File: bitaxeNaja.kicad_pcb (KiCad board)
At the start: 6 copper layers, 65 x 112 mm, 197 parts, among them J1 XT30, J2 Conn_01x08, J3 Conn_01x04, J4 USB_C_Receptacle_USB2.0, J7 Conn_01x04, J8 TC2030-IDC, SW1 SWITCH-SPST, SW2 SWITCH-SPST, U1 TPS546D24ARVFR, U11 MCP1824, U12 MCP1824, U13 EMC2103-2, U2 SN74AVC4T774, U3 TPSM861253RDXR, U4 TPS546D24ARVFR, U5 L78L05_SOT89, U6 ESP32-S3-WROOM-1, U8 25MHz

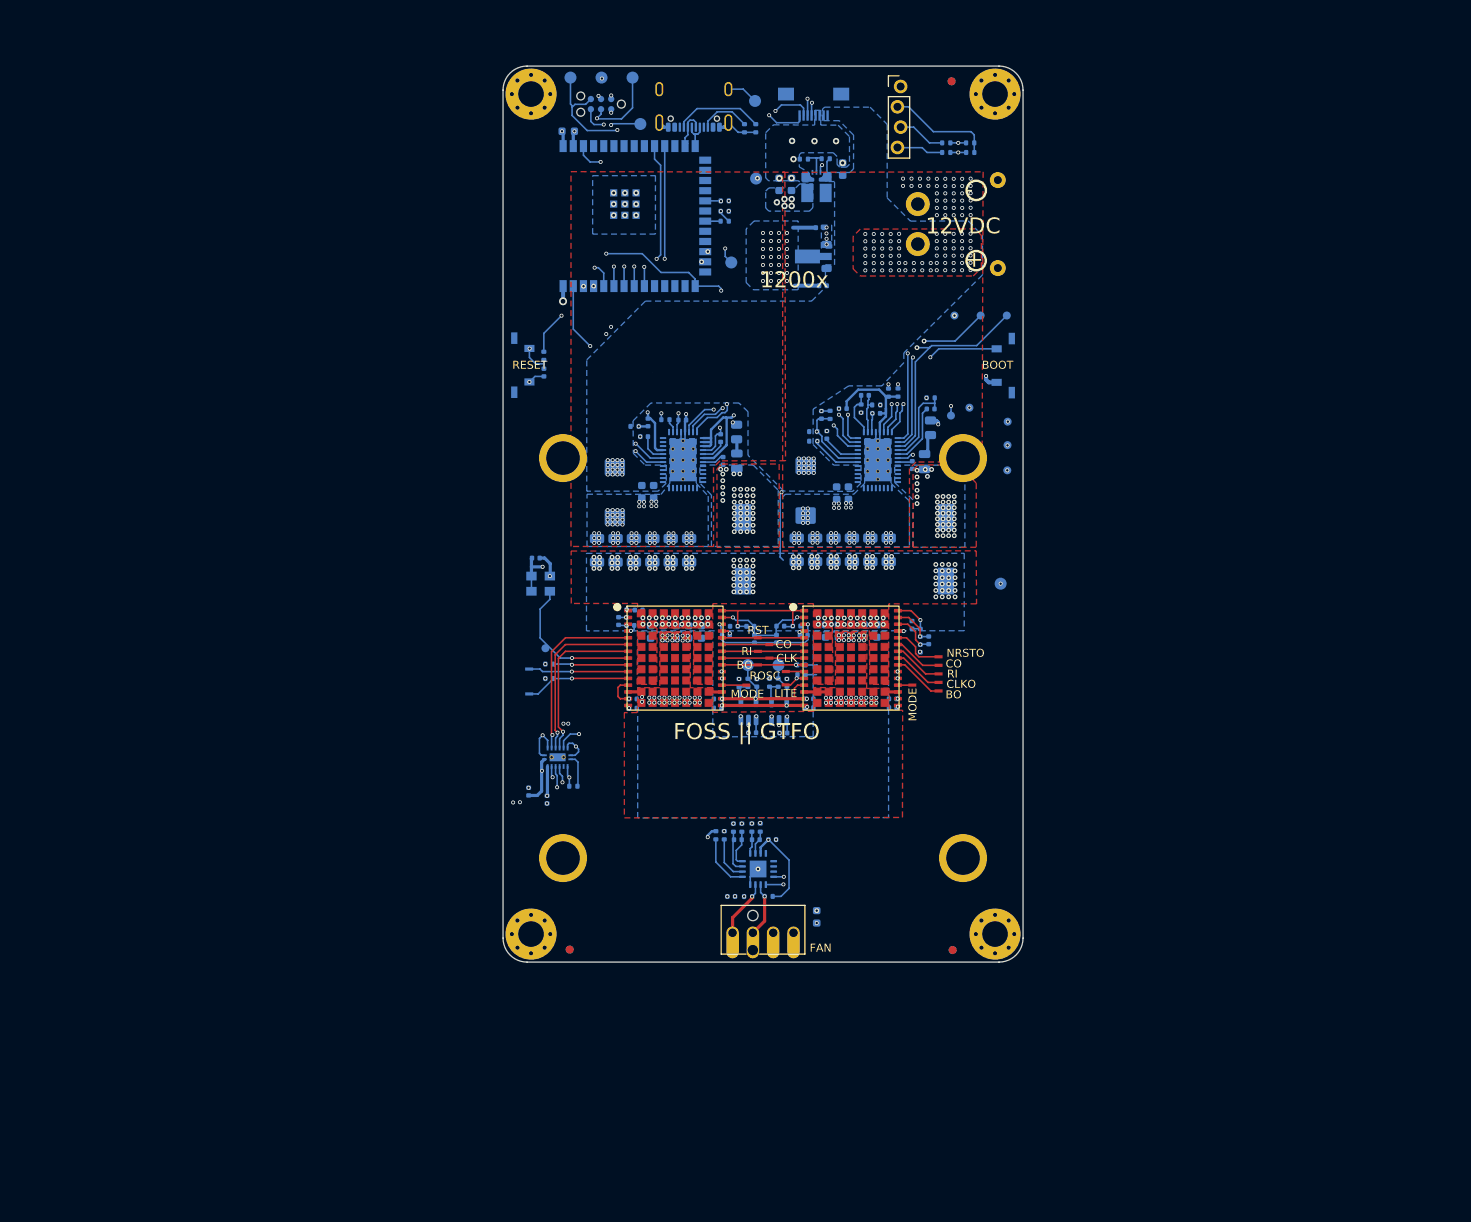
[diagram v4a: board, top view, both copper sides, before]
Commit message: switched to single phase TPS546D24 and put the ASICs in series.
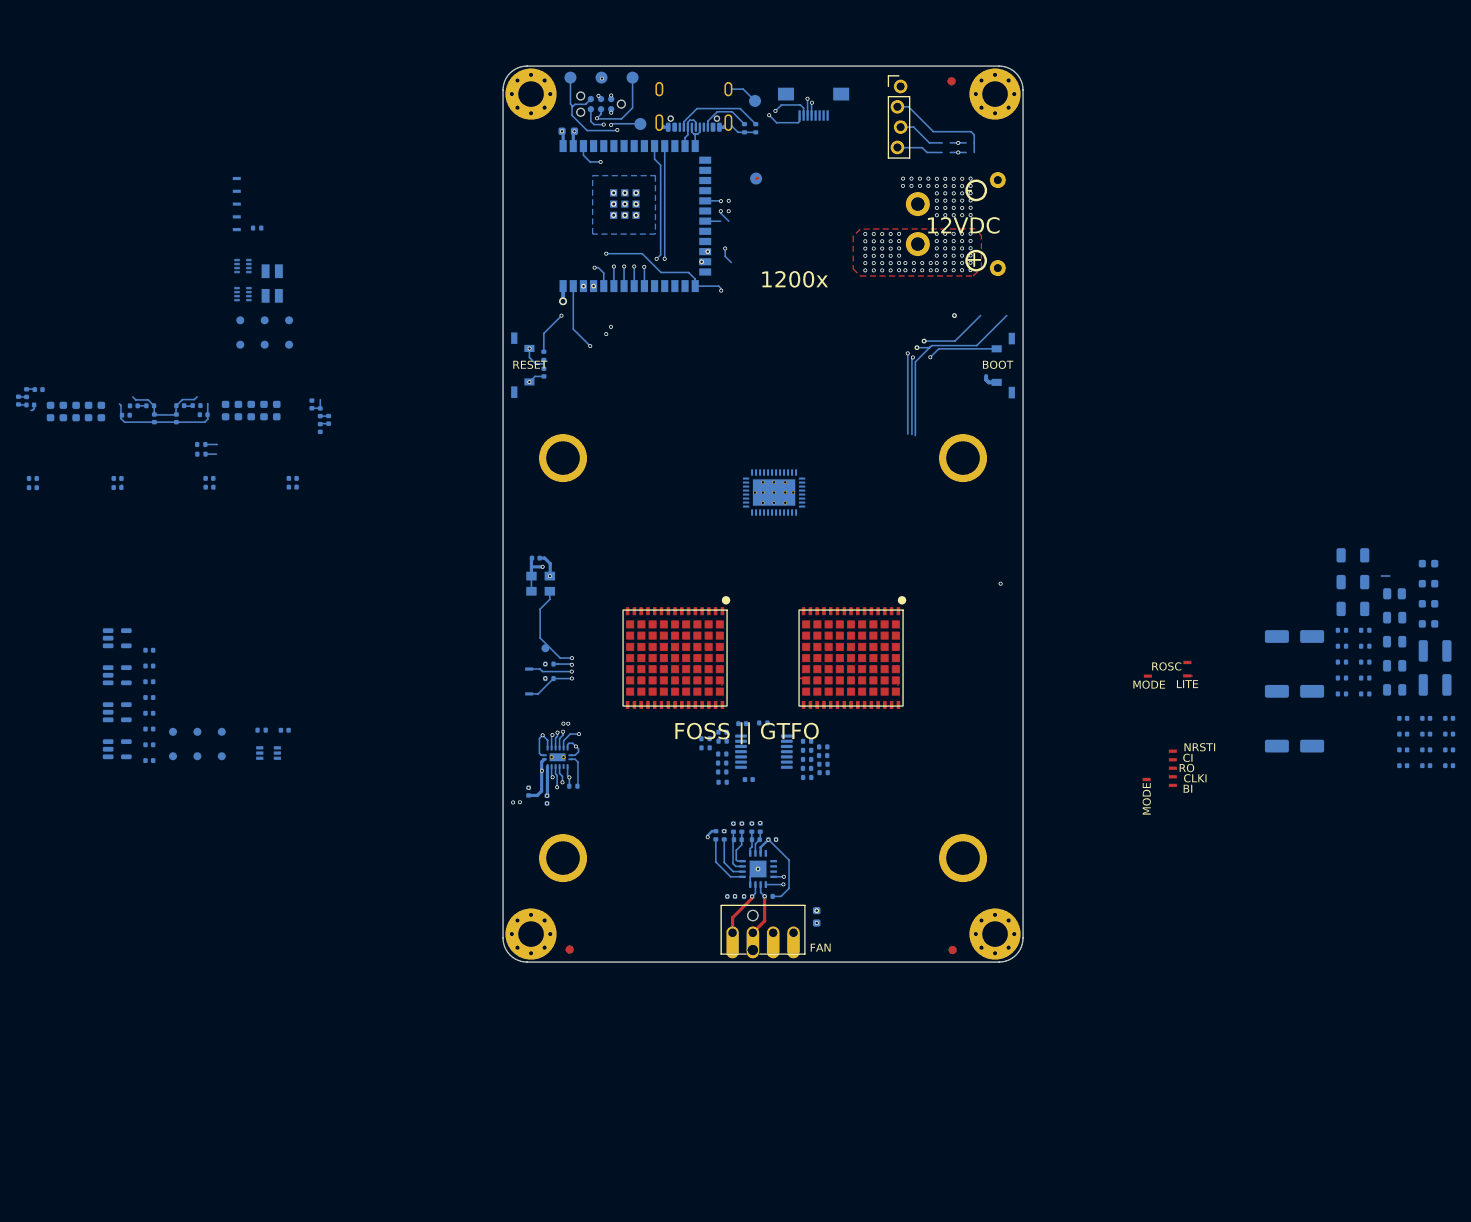
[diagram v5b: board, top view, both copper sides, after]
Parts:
- removed C20, C45: 33pF, Capacitor_SMD:C_0402_1005Metric
- removed C28: 0.1uF, Capacitor_SMD:C_0402_1005Metric
- removed C31, C32, C33: 100uF, Capacitor_SMD:C_1206_3216Metric
- removed C44: 10uF, Capacitor_SMD:C_0603_1608Metric
- removed C46, C47: 1uF, Capacitor_SMD:C_0402_1005Metric
- removed L1: 230nH, bitaxe:FP1107R1
- removed NT2: NetTie_2, bitaxe:NetTie-2_SMD_Pad0.2mmx1mm
- removed R1: 49.9, Resistor_SMD:R_0402_1005Metric
- removed R11: 46.4k, Resistor_SMD:R_0402_1005Metric
- removed R19: 10k, Resistor_SMD:R_0402_1005Metric
- removed R2: 1, Resistor_SMD:R_0805_2012Metric
- removed R21, R22, R40: 4.7k, Resistor_SMD:R_0402_1005Metric
- removed R39: 0, Resistor_SMD:R_0402_1005Metric
- removed R4: 6.04k, Resistor_SMD:R_0402_1005Metric
- removed R41: 38.3k, Resistor_SMD:R_0402_1005Metric
- removed R42, R44: 20k, Resistor_SMD:R_0402_1005Metric
- removed R43: 19.1k, Resistor_SMD:R_0402_1005Metric
- removed TP3: BCX_CLK, TestPoint:TestPoint_Pad_D1.0mm
- removed TP31: BCX_DAT, TestPoint:TestPoint_Pad_D1.0mm
- removed TP37: CO, bitaxe:TestPoint_Pad_1.0x0.4mm
- removed TP38: RI, bitaxe:TestPoint_Pad_1.0x0.4mm
- removed TP39: CLK, bitaxe:TestPoint_Pad_1.0x0.4mm
- removed TP40: BO, bitaxe:TestPoint_Pad_1.0x0.4mm
- removed U1: TPS546D24ARVFR, bitaxe:LQFN40-CLIP
- added C206: 0.1uF, Capacitor_SMD:C_0402_1005Metric, B.Cu at (128.4, 120.2)
- added C207: 1uF, Capacitor_SMD:C_0402_1005Metric, B.Cu at (129.2, 127.2)
- added C6: 4.7uF, Capacitor_SMD:C_1206_3216Metric, B.Cu at (204.7, 105.9)
- added C63: 1uF, Capacitor_SMD:C_0402_1005Metric, B.Cu at (54.3, 124.8)
- added C96: 1uF, Capacitor_SMD:C_0402_1005Metric, B.Cu at (54.3, 115.0)
- added C97: 1uF, Capacitor_SMD:C_0402_1005Metric, B.Cu at (54.3, 113.0)
- added C98: 1uF, Capacitor_SMD:C_0402_1005Metric, B.Cu at (54.3, 111.0)
- added L3: 1.5uH, bitaxe:IND-SMD_L2.0-W1.6, B.Cu at (69.6, 63.6)
- added R12: 30.9k, Resistor_SMD:R_0402_1005Metric, B.Cu at (203.4, 108.5)
- added R55: 1k, Resistor_SMD:R_0402_1005Metric, B.Cu at (126.0, 127.5)
- added R56: 10k, Resistor_SMD:R_0402_1005Metric, B.Cu at (125.9, 125.1)
- added R57: 10k, Resistor_SMD:R_0402_1005Metric, B.Cu at (125.9, 124.0)
- added R58: 1k, Resistor_SMD:R_0402_1005Metric, B.Cu at (125.9, 121.3)
- added R59: 10k, Resistor_SMD:R_0402_1005Metric, B.Cu at (123.8, 123.2)
- added R60: 10k, Resistor_SMD:R_0402_1005Metric, B.Cu at (123.8, 122.1)
- added R61: 1k, Resistor_SMD:R_0402_1005Metric, B.Cu at (138.5, 123.1)
- added R62: 10k, Resistor_SMD:R_0402_1005Metric, B.Cu at (136.5, 123.5)
- added R63: 10k, Resistor_SMD:R_0402_1005Metric, B.Cu at (138.5, 124.2)
- added R64: 1k, Resistor_SMD:R_0402_1005Metric, B.Cu at (136.5, 125.8)
- added R65: 10k, Resistor_SMD:R_0402_1005Metric, B.Cu at (136.5, 126.9)
- added R66: 10k, Resistor_SMD:R_0402_1005Metric, B.Cu at (138.6, 126.3)
- added R67: 0, Resistor_SMD:R_0402_1005Metric, B.Cu at (131.0, 120.1)
- added R68: 1k, Resistor_SMD:R_0402_1005Metric, B.Cu at (125.9, 126.2)
- added R69: 1k, Resistor_SMD:R_0402_1005Metric, B.Cu at (126.0, 122.4)
- added R70: 1k, Resistor_SMD:R_0402_1005Metric, B.Cu at (136.5, 122.4)
- added R71: 1k, Resistor_SMD:R_0402_1005Metric, B.Cu at (136.5, 124.7)
- added R72: 1k, Resistor_SMD:R_0402_1005Metric, B.Cu at (138.6, 125.3)
- added TP14: 3V3, bitaxe:TestPoint_Pad_D1.0mm, B.Cu at (65.7, 69.8)
- added TP16: VDD, bitaxe:TestPoint_Pad_D1.0mm, B.Cu at (68.7, 69.8)
- added TP17: BO, bitaxe:TestPoint_Pad_1.0x0.4mm, B.Cu at (65.2, 58.4)
- added TP20: GND, bitaxe:TestPoint_Pad_D1.0mm, B.Cu at (71.8, 72.8)
- added TP21: GND, bitaxe:TestPoint_Pad_D1.0mm, B.Cu at (71.8, 69.8)
- added TP28: 0V8, bitaxe:TestPoint_Pad_D1.0mm, B.Cu at (63.3, 124.3)
- added U10: TLV77308PDBVR, Package_TO_SOT_SMD:SOT-23-5, B.Cu at (50.3, 123.4)
- added U14: TLV77312PDBVR, Package_TO_SOT_SMD:SOT-23-5, B.Cu at (50.3, 109.5)
- added U17: TLV3544, Package_SO:TSSOP-14_4.4x5mm_P0.65mm, B.Cu at (131.1, 123.7)
- added U9: TPS22919DCKR, bitaxe:DCK0006A_N, B.Cu at (69.2, 123.9)
- C1: value 33uF -> 68uF; footprint Capacitor_Tantalum_SMD:CP_EIA-7343-31_Kemet-D -> Capacitor_SMD:CP_Elec_5x5.8
- C10, C9: value 100uF -> 1uF; footprint Capacitor_SMD:C_1206_3216Metric -> Capacitor_SMD:C_0603_1608Metric
- C11: value 100uF -> 4.7uF; footprint Capacitor_SMD:C_1206_3216Metric -> Capacitor_SMD:C_0402_1005Metric
- C12: value 100uF -> 10uF; footprint Capacitor_SMD:C_1206_3216Metric -> Capacitor_SMD:C_0603_1608Metric
- C13: value 100uF -> 4.7nF; footprint Capacitor_SMD:C_1206_3216Metric -> Capacitor_SMD:C_0402_1005Metric
- C14: value 100uF -> 2.2nF; footprint Capacitor_SMD:C_1206_3216Metric -> Capacitor_SMD:C_0402_1005Metric
- C16, C37: value 4.7uF -> 0.1uF
- C17: value 0.1uF -> 1000pF; footprint Capacitor_SMD:C_0402_1005Metric -> Capacitor_SMD:C_0805_2012Metric
- C19: value 1uF -> 4.7uF; footprint Capacitor_SMD:C_0402_1005Metric -> Capacitor_SMD:C_1206_3216Metric
- C2, C3: value 10uF -> 68uF; footprint Capacitor_SMD:C_0603_1608Metric -> Capacitor_SMD:CP_Elec_5x5.8
- C22: value 33uF -> 47uF; footprint Capacitor_Tantalum_SMD:CP_EIA-7343-31_Kemet-D -> Capacitor_SMD:C_0805_2012Metric
- C23, C24: value 10uF -> 100uF; footprint Capacitor_SMD:C_0603_1608Metric -> Capacitor_SMD:C_1210_3225Metric
- C29: value 1000pF -> 33nF; footprint Capacitor_SMD:C_0805_2012Metric -> Capacitor_SMD:C_0402_1005Metric
- C30: value 100uF -> 33nF; footprint Capacitor_SMD:C_1206_3216Metric -> Capacitor_SMD:C_0402_1005Metric
- C34: value 100uF -> 1uF; footprint Capacitor_SMD:C_1206_3216Metric -> Capacitor_SMD:C_0402_1005Metric
- C35: value 100uF -> 22uF; footprint Capacitor_SMD:C_1206_3216Metric -> Capacitor_SMD:C_0805_2012Metric
- C36: value 1uF -> 22uF; footprint Capacitor_SMD:C_0402_1005Metric -> Capacitor_SMD:C_0805_2012Metric
- C39, C43: value 10uF -> 0.1uF; footprint Capacitor_SMD:C_0603_1608Metric -> Capacitor_SMD:C_0402_1005Metric
- C42: value 1uF -> 0.1uF
- C7: value 0.1uF -> 4.7uF; footprint Capacitor_SMD:C_0402_1005Metric -> Capacitor_SMD:C_1206_3216Metric
- C8: value 1000pF -> 10uF; footprint Capacitor_SMD:C_0805_2012Metric -> Capacitor_SMD:C_0603_1608Metric
- L2: value 230nH -> 1.5uH; footprint bitaxe:FP1107R1 -> bitaxe:IND-SMD_L2.0-W1.6
- R13: value 31.6k -> 10k
- R15: value 1 -> 13.7k; footprint Resistor_SMD:R_0805_2012Metric -> Resistor_SMD:R_0402_1005Metric
- R16, R3: value 10 -> 10k
- R17: value 20k -> 52.3k
- R18: value 10k -> 1k
- R37: value 0 -> 10k
- R38: value 0 -> 1k
- R5: value 649 -> 10
- R6: value 10k -> 1; footprint Resistor_SMD:R_0402_1005Metric -> Resistor_SMD:R_0805_2012Metric
- R7: value 31.6k -> 49.9
- TP1: value TestPoint -> PWR EN; footprint TestPoint:TestPoint_Pad_D1.0mm -> bitaxe:TestPoint_Pad_D1.0mm
- TP15: value Vcore -> 5V; footprint TestPoint:TestPoint_Pad_D1.5mm -> bitaxe:TestPoint_Pad_D1.0mm
- TP18: value 1V2 -> CLKO; footprint TestPoint:TestPoint_Pad_D1.5mm -> bitaxe:TestPoint_Pad_1.0x0.4mm
- TP19: value 0V8 -> RI; footprint TestPoint:TestPoint_Pad_D1.5mm -> bitaxe:TestPoint_Pad_1.0x0.4mm
- TP22: value ALRT_VR -> CO; footprint TestPoint:TestPoint_Pad_D1.0mm -> bitaxe:TestPoint_Pad_1.0x0.4mm
- TP23: value SDA_VR -> NRSTO; footprint TestPoint:TestPoint_Pad_D1.0mm -> bitaxe:TestPoint_Pad_1.0x0.4mm
- TP24: value SCL_VR -> GND; footprint TestPoint:TestPoint_Pad_D1.0mm -> bitaxe:TestPoint_Pad_D1.0mm
- TP25: value GND -> 0V8; footprint TestPoint:TestPoint_Pad_D1.0mm -> bitaxe:TestPoint_Pad_D1.0mm
- TP26: value RST -> 1V2; footprint bitaxe:TestPoint_Pad_1.0x0.4mm -> bitaxe:TestPoint_Pad_D1.0mm; moved to B.Cu
- TP27: value 5V -> GND; footprint TestPoint:TestPoint_Pad_D1.5mm -> bitaxe:TestPoint_Pad_D1.0mm
- TP30: value BCX_CLK -> 1V2; footprint TestPoint:TestPoint_Pad_D1.0mm -> bitaxe:TestPoint_Pad_D1.0mm
- TP5: value BO -> BI
- TP6: value CLKO -> CLKI
- TP7: value RI -> RO
- TP8: value CO -> CI
- TP9: value NRSTO -> NRSTI
- U11: value MCP1824 -> TLV77312PDBVR
- U12: value MCP1824 -> TLV77308PDBVR
- U3: value TPSM861253RDXR -> TPS546D24SRVFR; footprint bitaxe:TPSM863257RDX -> bitaxe:LQFN40-CLIP
- U4: value TPS546D24ARVFR -> TPS62933DRLR; footprint bitaxe:LQFN40-CLIP -> bitaxe:SOT-583-8_L2.1-W1.2-P0.50-LS1.6-BR
- U5: value L78L05_SOT89 -> TPS62933DRLR; footprint Package_TO_SOT_SMD:SOT-89-3 -> bitaxe:SOT-583-8_L2.1-W1.2-P0.50-LS1.6-BR
- moved TP24 117.9 mm to (57.2, 124.3), turned to 0 degrees
- moved TP25 109.3 mm to (57.2, 121.2), turned to 0 degrees
- moved C37 108.7 mm to (216.8, 125.4)
- moved C43 105.9 mm to (216.8, 119.5), turned to 0 degrees
- moved C39 105.0 mm to (216.8, 123.5), turned to 0 degrees
- moved TP30 101.9 mm to (63.3, 121.2), turned to 0 degrees
- moved C24 101.1 mm to (215.0, 111.1), turned to 0 degrees
- moved C23 100.6 mm to (215.0, 115.4), turned to 0 degrees
- moved C35 100.4 mm to (210.0, 110.0), turned to 0 degrees
- moved C22 99.9 mm to (210.0, 113.0), turned to 0 degrees
- moved R18 98.4 mm to (68.3, 121.0)
- moved C42 98.3 mm to (216.8, 121.5), turned to 0 degrees
- moved R6 97.1 mm to (209.9, 104.0)
- moved TP15 96.7 mm to (68.7, 72.8)
- moved C36 96.5 mm to (210.0, 106.9), turned to 0 degrees
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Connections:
- A1 pad 12: /ASIC/0V8_1 -> /ASIC/0V8_0
- A1 pad 14: /ASIC/0V8_1 -> /ASIC/0V8_0
- A1 pad 15: /ASIC/1V2_1 -> /ASIC/1V2_0
- A1 pad 16: /ASIC/1V2 -> /ASIC/1V2_0
- A1 pad 17: /ASIC/0V8 -> /ASIC/0V8_0
- A1 pad 22: Net-(A1-BO) -> /ASIC/Level Shifter/BI
- A1 pad 23: Net-(A1-CLKO) -> /ASIC/Level Shifter/CLKI
- A1 pad 24: Net-(A1-RI) -> /ASIC/Level Shifter/RO
- A1 pad 25: Net-(A1-CO) -> /ASIC/Level Shifter/CI
- A1 pad 26: Net-(A1-NRSTO) -> /ASIC/Level Shifter/NRSTI
- A1 pad 27: GND -> Net-(A1-VSS-Pad27)
- A1 pad 31: /Vcore -> /ASIC/GND_1
- A2 pad 1: Net-(A1-VDD3_1) -> Net-(A2-VDD3_0)
- A2 pad 12: /ASIC/0V8 -> Net-(A2-INV_CLKO)
- A2 pad 13: GND -> /ASIC/GND_1
- A2 pad 14: /ASIC/0V8 -> Net-(A2-INV_CLKO)
- A2 pad 15: /ASIC/1V2 -> Net-(A2-VDDIO_12_0)
- A2 pad 16: /ASIC/1V2_2 -> /ASIC/1V2_1
- A2 pad 17: /ASIC/0V8_2 -> /ASIC/0V8_1
- A2 pad 18: GND -> /ASIC/GND_1
- A2 pad 19: Net-(A2-PIN_MODE) -> /ASIC/GND_1
- A2 pad 2: Net-(A1-VDD2_1) -> Net-(A2-VDD2_0)
- A2 pad 22: Net-(A2-BO) -> /ASIC/Level Shifter/NRSTI2
- A2 pad 23: Net-(A2-CLKO) -> /ASIC/Level Shifter/CI2
- A2 pad 24: Net-(A2-RI) -> /ASIC/Level Shifter/RO2
- A2 pad 25: Net-(A2-CO) -> /ASIC/Level Shifter/CLKO
- A2 pad 26: Net-(A2-NRSTO) -> /ASIC/Level Shifter/BI2
- A2 pad 27: GND -> /ASIC/GND_1
- A2 pad 3: Net-(A1-VDD1_1) -> Net-(A2-VDD1_0)
- A2 pad 31: /Vcore -> /VDD
- A2 pad 32: GND -> /ASIC/GND_1
- A2 pad 4: GND -> /ASIC/GND_1
- A2 pad 5: Net-(A1-NRSTO) -> unconnected-(A2-BO-Pad5)
- A2 pad 6: Net-(A1-CO) -> unconnected-(A2-CLKO-Pad6)
- A2 pad 7: Net-(A1-RI) -> Net-(A2-RI)
- A2 pad 8: Net-(A1-CLKO) -> unconnected-(A2-CO-Pad8)
- A2 pad 9: Net-(A1-BO) -> unconnected-(A2-NRSTO-Pad9)
- C10 pad 1: GND -> /Power/AGND
- C10 pad 2: /Vcore -> Net-(U3-AVIN)
- C11 pad 2: /Vcore -> /Power/V5reg_1
- C12 pad 2: /Vcore -> /12V
- C13 pad 1: GND -> /12V
- C13 pad 2: /Vcore -> GND
- C14 pad 1: GND -> /12V
- C14 pad 2: /Vcore -> GND
- C15 pad 1: /Power/AGND1 -> /Power/BP1v5
- C15 pad 2: Net-(U1-AVIN) -> Net-(U3-DRTN)
- C16 pad 1: GND -> Net-(U3-BOOT)
- C16 pad 2: /Power/V5reg_1 -> /Power/SW1
- C17 pad 1: /Power/EN_UVLO -> /Power/SW1
- C17 pad 2: GND -> Net-(C17-Pad2)
- C18 pad 1: Net-(U1-VOSNS) -> Net-(U3-VOSNS)
- C18 pad 2: Net-(U1-GOSNS) -> Net-(U3-GOSNS)
- C19 pad 1: /Power/BP1v5_1 -> /12V
- C19 pad 2: Net-(U1-DRTN) -> GND
- C22 pad 1: /12V -> GND
- C22 pad 2: GND -> /VDD
- C23 pad 1: /12V -> GND
- C23 pad 2: GND -> /VDD
- C24 pad 1: /12V -> GND
- C24 pad 2: GND -> /VDD
- C29 pad 1: /Power/SW2 -> GND
- C29 pad 2: Net-(C29-Pad2) -> Net-(U4-SS)
- C30 pad 2: /Vcore -> Net-(U5-SS)
- C34 pad 1: GND -> /5V
- C34 pad 2: /Vcore -> GND
- C35 pad 2: /Vcore -> /3V3
- C36 pad 1: /Power/AGND2 -> GND
- C36 pad 2: Net-(U4-AVIN) -> /5V
- C37 pad 1: GND -> /12V
- C37 pad 2: /Power/V5reg_2 -> GND
- C38 pad 1: /Vcore -> /ASIC/GND_1
- C42 pad 1: /Power/BP1v5_2 -> Net-(U4-BST)
- C42 pad 2: Net-(U4-DRTN) -> Net-(U4-SW)
- C43 pad 1: /3V3 -> Net-(U5-BST)
- C43 pad 2: GND -> Net-(U5-SW)
- C51 pad 1: /ASIC/1V2 -> /ASIC/1V2_0
- C53 pad 1: /ASIC/1V2 -> /ASIC/1V2_0
- C54 pad 1: /Vcore -> /ASIC/GND_1
- C55 pad 1: /Vcore -> /ASIC/GND_1
- C56 pad 1: /Vcore -> /ASIC/GND_1
- C57 pad 1: /Vcore -> /ASIC/GND_1
- C58 pad 1: /Vcore -> /VDD
- C58 pad 2: GND -> /ASIC/GND_1
- C59 pad 1: /Vcore -> /VDD
- C59 pad 2: GND -> /ASIC/GND_1
- C60 pad 1: /Vcore -> /VDD
- C60 pad 2: GND -> /ASIC/GND_1
- C61 pad 1: /Vcore -> /VDD
- C61 pad 2: GND -> /ASIC/GND_1
- C62 pad 1: /Vcore -> /VDD
- C62 pad 2: GND -> /ASIC/GND_1
- C67 pad 2: /Vcore -> /ASIC/GND_1
- C68 pad 1: /Vcore -> /ASIC/GND_1
- C7 pad 1: Net-(U1-BOOT) -> /12V
- C7 pad 2: /Power/SW1 -> GND
- C71 pad 2: GND -> Net-(A1-VSS-Pad27)
- C72 pad 1: GND -> /ASIC/GND_1
- C72 pad 2: Net-(A1-VDD1_1) -> Net-(A2-VDD1_0)
- C73 pad 1: Net-(A1-VDD1_1) -> Net-(A2-VDD1_0)
- C73 pad 2: Net-(A1-VDD2_1) -> Net-(A2-VDD2_0)
- C74 pad 1: Net-(A1-VDD2_1) -> Net-(A2-VDD2_0)
- C74 pad 2: Net-(A1-VDD3_1) -> Net-(A2-VDD3_0)
- C75 pad 1: Net-(A1-VDD3_1) -> Net-(A2-VDD3_0)
- C75 pad 2: /Vcore -> /VDD
- C76 pad 1: /Vcore -> /VDD
- C79 pad 2: GND -> /ASIC/GND_1
- C8 pad 1: /Power/SW1 -> GND
- C8 pad 2: Net-(C8-Pad2) -> /12V
- C80 pad 2: /ASIC/0V8_1 -> /ASIC/0V8_0
- C81 pad 2: /ASIC/1V2_1 -> /ASIC/1V2_0
- C82 pad 2: /ASIC/0V8 -> /ASIC/0V8_0
- C83 pad 2: /ASIC/1V2 -> /ASIC/1V2_0
- C84 pad 1: GND -> /ASIC/GND_1
- C84 pad 2: /ASIC/1V2 -> Net-(A2-VDDIO_12_0)
- C85 pad 1: GND -> /ASIC/GND_1
- C85 pad 2: /ASIC/0V8 -> Net-(A2-INV_CLKO)
- C86 pad 1: GND -> /ASIC/GND_1
- C86 pad 2: /ASIC/1V2_2 -> /ASIC/1V2_1
- C87 pad 1: GND -> /ASIC/GND_1
- C87 pad 2: /ASIC/0V8_2 -> /ASIC/0V8_1
- C88 pad 2: /5V -> /ASIC/5V_SWITCH
- C89 pad 2: /ASIC/1V2 -> /ASIC/0V8_0
- C9 pad 1: GND -> /12V
- C9 pad 2: /Vcore -> GND
- C90 pad 2: /5V -> /ASIC/1V2_0
- C91 pad 1: GND -> /ASIC/GND_1
- C91 pad 2: /ASIC/0V8 -> /ASIC/5V_SWITCH
- L2 pad 1: /Power/SW2 -> Net-(U4-SW)
- L2 pad 2: /Vcore -> /3V3
- NT1 pad 2: /Power/AGND1 -> /Power/AGND
- R13 pad 1: /Power/AGND1 -> GND
- R13 pad 2: Net-(U1-VSEL) -> Net-(U4-FB)
- R15 pad 1: Net-(C29-Pad2) -> GND
- R15 pad 2: GND -> Net-(U4-RT)
- R16 pad 1: /12V -> GND
- R16 pad 2: Net-(U4-AVIN) -> Net-(U5-RT)
- R17 pad 1: Net-(U3-EN) -> Net-(U5-FB)
- R17 pad 2: /12V -> /5V
- R18 pad 1: GND -> /ESP32/5V_SWITCH
- R18 pad 2: Net-(U3-EN) -> Net-(U9-QOD)
- R27 pad 2: Net-(A1-BO) -> /ASIC/Level Shifter/BI
- R28 pad 1: GND -> /ASIC/GND_1
- R3 pad 1: /12V -> GND
- R3 pad 2: Net-(U1-AVIN) -> /ESP32/PWR_EN
- R37 pad 1: /ESP32/SMB_ALRT -> GND
- R37 pad 2: /Power/ALRT_VR -> Net-(U5-FB)
- R38 pad 1: /ESP32/SDA -> Net-(A2-RI)
- R38 pad 2: /Power/SDA_VR -> /ASIC/1V2_1
- R5 pad 1: GND -> /12V
- R5 pad 2: /Power/EN_UVLO -> Net-(U3-AVIN)
- R6 pad 1: /Power/PGOOD -> Net-(C17-Pad2)
- R6 pad 2: /3V3 -> GND
- R7 pad 1: Net-(U1-MSEL1) -> /VDD
- R7 pad 2: /Power/BP1v5_1 -> Net-(U3-VOSNS)
- R8 pad 1: Net-(U1-GOSNS) -> Net-(U3-GOSNS)
- TP1 pad 1: Net-(U1-ADRSEL) -> /ESP32/PWR_EN
- TP15 pad 1: /Vcore -> /5V
- TP18 pad 1: /ASIC/1V2 -> /ASIC/Level Shifter/CLKI
- TP19 pad 1: /ASIC/0V8 -> /ASIC/Level Shifter/RO
- TP22 pad 1: /Power/ALRT_VR -> /ASIC/Level Shifter/CI
- TP23 pad 1: /Power/SDA_VR -> /ASIC/Level Shifter/NRSTI
- TP24 pad 1: /Power/SCL_VR -> GND
- TP25 pad 1: GND -> /ASIC/0V8_0
- TP26 pad 1: Net-(A1-NRSTO) -> /ASIC/1V2_0
- TP27 pad 1: /5V -> /ASIC/GND_1
- TP30 pad 1: /Power/BCX_CLK -> /ASIC/1V2_1
- TP42 pad 1: Net-(A2-PIN_MODE) -> /ASIC/GND_1
- TP5 pad 1: Net-(A2-BO) -> /ASIC/Level Shifter/BI2
- TP6 pad 1: Net-(A2-CLKO) -> /ASIC/Level Shifter/CLKO
- TP7 pad 1: Net-(A2-RI) -> /ASIC/Level Shifter/RO2
- TP8 pad 1: Net-(A2-CO) -> /ASIC/Level Shifter/CI2
- TP9 pad 1: Net-(A2-NRSTO) -> /ASIC/Level Shifter/NRSTI2
- U11 pad 1: /5V -> /ASIC/5V_SWITCH
- U11 pad 3: /5V -> /ASIC/5V_SWITCH
- U11 pad 4: Net-(U11-ADJ) -> unconnected-(U11-NC-Pad4)
- U11 pad 5: /ASIC/1V2 -> /ASIC/1V2_0
- U12 pad 1: /5V -> /ASIC/5V_SWITCH
- U12 pad 2: GND -> /ASIC/GND_1
- U12 pad 3: /5V -> /ASIC/5V_SWITCH
- U12 pad 4: Net-(U12-ADJ) -> unconnected-(U12-NC-Pad4)
- U12 pad 5: /ASIC/0V8 -> /ASIC/0V8_1
- U2 pad 16: /ASIC/1V2 -> /ASIC/1V2_0
- U3 pad 1: /12V -> /Power/PGOOD
- U3 pad 2: unconnected-(U3-SW-Pad2) -> /ESP32/SDA
- U3 pad 3: /3V3 -> /ESP32/SCL
- U3 pad 4: GND -> /Power/BP1v5
- U3 pad 5: unconnected-(U3-PG-Pad5) -> Net-(U3-DRTN)
- U3 pad 6: Net-(U3-EN) -> /ESP32/SMB_ALRT
- U3 pad 7: /3V3 -> Net-(U3-BOOT)
- U4 pad 1: /Power/AGND2 -> Net-(U4-RT)
- U4 pad 2: /Power/AGND2 -> unconnected-(U4-EN-Pad2)
- U4 pad 3: /Power/AGND2 -> /12V
- U4 pad 4: /Power/BP1v5_2 -> GND
- U4 pad 5: Net-(U4-DRTN) -> Net-(U4-SW)
- U4 pad 6: /Power/AGND2 -> Net-(U4-BST)
- U4 pad 7: Net-(U4-BOOT) -> Net-(U4-SS)
- U4 pad 8: /Power/SW2 -> Net-(U4-FB)
- U5 pad 1: /5V -> Net-(U5-RT)
- U5 pad 2: GND -> unconnected-(U5-EN-Pad2)
- U6 pad 23: unconnected-(U6-GPIO21-Pad23) -> /ESP32/5V_EN
- U6 pad 38: /Vcore -> /VDD
- U8 pad 1: /ASIC/1V2 -> /ASIC/1V2_0
- U8 pad 4: /ASIC/1V2 -> /ASIC/1V2_0
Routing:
- net (no net): track 0.00 -> 178.4 mm, vias 0 -> 8
- net /Vcore: track 73.6 -> 0.00 mm, vias 168 -> 0
- net /Power/SCL_VR: track 72.3 -> 0.00 mm, vias 2 -> 0
- net /Power/ALRT_VR: track 66.9 -> 0.00 mm, vias 3 -> 0
- net /Power/SDA_VR: track 66.6 -> 0.00 mm, vias 3 -> 0
- net /Power/SYNC: track 49.3 -> 0.00 mm, vias 3 -> 0
- net /Power/BCX_DAT: track 49.1 -> 0.00 mm, vias 3 -> 0
- net /ASIC/1V2: track 94.0 -> 46.6 mm, vias 6 -> 3
- net /VDD: track 0.00 -> 42.8 mm, vias 0 -> 1
- net /Power/BCX_CLK: track 42.8 -> 0.00 mm, vias 3 -> 0
- net /Power/AGND2: track 42.3 -> 0.00 mm, vias 3 -> 0
- net /Power/EN_UVLO: track 40.6 -> 0.00 mm, vias 2 -> 0
- net /Power/VSHARE: track 32.9 -> 0.00 mm, vias 2 -> 0
- net /5V: track 162.8 -> 130.9 mm, vias 13 -> 5
- net GND: track 68.2 -> 38.9 mm, vias 302 -> 64
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- removed copper zone on B.Cu, net /12V
- removed copper zone on In2.Cu, net /12V
- removed copper zone on B.Cu, net /3V3
- removed copper zone on B.Cu, net /5V
- removed copper zone on B.Cu, net /Power/SW1
- removed copper zone on F.Cu, net /Power/SW1
- removed copper zone on In2.Cu, net /Power/SW1
- removed copper zone on B.Cu, net /Power/SW2
- removed copper zone on F.Cu, net /Power/SW2
- removed copper zone on In2.Cu, net /Power/SW2
- removed copper zone on B.Cu, net /Vcore
- removed copper zone on F.Cu, net /Vcore
- removed copper zone on In2.Cu, net /Vcore
- removed copper zone on F.Cu, net GND
- removed copper zone on In2.Cu, net GND
- removed copper zone on In3.Cu, net GND

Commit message: rough parts placement.
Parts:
- removed H5, H6, H7, H8: MountingHole_Pad, bitaxe:Sinhoo SMTSO3015CTJ_nopaste
- added C99: 0.1uF, Capacitor_SMD:C_0402_1005Metric, B.Cu at (164.2, 128.8)
- added HS1: Heatsink, bitaxe:Heatsink-5hole-BitaxeGT, F.Cu at (131.0, 112.0)
- added L1: 150nH, bitaxe:GDIM107050-R15S1MTF-0R37, B.Cu at (133.4, 100.5)
- added R73: 0, Resistor_SMD:R_0402_1005Metric, B.Cu at (156.9, 128.5)
- added TP31: CLKI, TestPoint:TestPoint_Pad_D1.0mm, B.Cu at (159.4, 123.5)
- added U1: STHW4-DU-HN050206, bitaxe:PAD-SMD_L5.0-W2.0_STHW4-DU-HN050206, F.Cu at (132.4, 91.3)
- added U15: 25MHz, bitaxe:SMD3225-4P, B.Cu at (160.5, 127.8)
- TP17, TP18, TP19, TP22, TP23: moved to F.Cu
- moved C37 161.8 mm to (75.5, 46.5), turned to 90 degrees
- moved C42 161.2 mm to (76.5, 42.2), turned to 180 degrees
- moved C29 156.9 mm to (78.1, 42.9), turned to -90 degrees
- moved C35 150.9 mm to (73.3, 46.0), turned to 180 degrees
- moved C8 149.2 mm to (77.8, 47.2), turned to 180 degrees
- moved C39 147.4 mm to (82.3, 63.2), turned to 90 degrees
- moved C43 146.6 mm to (83.3, 58.9), turned to 180 degrees
- moved R13 145.4 mm to (79.8, 44.7), turned to 180 degrees
- moved R15 143.9 mm to (79.8, 45.8), turned to 180 degrees
- moved C30 142.2 mm to (84.9, 59.6), turned to -90 degrees
- moved R12 139.6 mm to (79.8, 43.5)
- moved C36 137.3 mm to (80.0, 62.7), turned to 180 degrees
- moved C12 134.4 mm to (84.7, 64.0), turned to 180 degrees
- moved R17 129.9 mm to (86.5, 60.3)
- moved R16 129.9 mm to (86.4, 62.5), turned to 180 degrees
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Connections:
- A1 pad 27: Net-(A1-VSS-Pad27) -> GND
- A2 pad 12: Net-(A2-INV_CLKO) -> /ASIC/0V8_1
- A2 pad 14: Net-(A2-INV_CLKO) -> /ASIC/0V8_1
- A2 pad 15: Net-(A2-VDDIO_12_0) -> /ASIC/1V2_1
- C71 pad 2: Net-(A1-VSS-Pad27) -> GND
- C84 pad 2: Net-(A2-VDDIO_12_0) -> /ASIC/1V2_1
- C85 pad 2: Net-(A2-INV_CLKO) -> /ASIC/0V8_1
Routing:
- net /5V: track 130.9 -> 1.22 mm, vias 5 -> 3
- net /3V3: track 133.5 -> 14.2 mm, vias 8 -> 5
- net (no net): track 178.4 -> 62.1 mm, vias 8 -> 1
- net /ESP32/SCL: track 163.7 -> 53.1 mm, vias 4 -> 2
- net /ESP32/SDA: track 161.4 -> 54.4 mm, vias 4 -> 2
- net /12V: track 102.1 -> 0.01 mm, vias 69 -> 0
- net /ASIC/RX_3V3: track 93.5 -> 15.5 mm
- net /ASIC/TX_3V3: track 94.5 -> 16.8 mm
- net /ASIC/RST_3V3: track 70.0 -> 0.70 mm, vias 2 -> 1
- net /ASIC/1V2: track 46.6 -> 0.02 mm, vias 3 -> 0
- net /ESP32/IO0: track 89.2 -> 59.2 mm, vias 4 -> 3
- net /Power/PGOOD: track 47.9 -> 26.2 mm, vias 2 -> 1
- net GND: track 38.9 -> 21.7 mm, vias 64 -> 20
- net Net-(A1-VDD1_1): track 15.0 -> 0.00 mm
- net /ASIC/CLKI: track 11.4 -> 0.00 mm, vias 1 -> 0
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- added copper zone on B.Cu, net /12V
- added copper zone on B.Cu, net /3V3
- added copper zone on B.Cu, net /5V
- added copper zone on B.Cu, net /ASIC/GND_1
- added copper zone on F.Cu, net /ASIC/GND_1
- added copper zone on B.Cu, net /Power/SW1
- added copper zone on B.Cu, net /VDD
- added copper zone on F.Cu, net /VDD
- added copper zone on F.Cu, net GND
- added copper zone on B.Cu, net Net-(U4-SW)
- added copper zone on B.Cu, net Net-(U5-SW)
- removed copper zone on In3.Cu, net /12V
- removed copper zone on In4.Cu, net /3V3
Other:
- board text added: "1201x"
- board text removed: "1200x"

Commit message: finished placing parts. lots of routing.
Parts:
- removed J8: TC2030-IDC, Connector:Tag-Connect_TC2030-IDC-NL_2x03_P1.27mm_Vertical
- removed TP29: EN, TestPoint:TestPoint_Pad_D1.5mm
- removed TP32: TX, TestPoint:TestPoint_Pad_D1.5mm
- removed TP33: RX, TestPoint:TestPoint_Pad_D1.5mm
- removed TP34: 3V3, TestPoint:TestPoint_Pad_D1.5mm
- removed TP35: GND, TestPoint:TestPoint_Pad_D1.5mm
- removed TP36: IO0, TestPoint:TestPoint_Pad_D1.5mm
- moved SW2 100.9 mm to (111.3, 40.3), turned to 0 degrees
- moved TP28 86.6 mm to (149.9, 128.5)
- moved TP27 81.7 mm to (151.8, 126.0)
- moved TP30 80.1 mm to (143.1, 128.1)
- moved SW1 74.8 mm to (161.2, 58.2)
- moved R20 72.6 mm to (157.9, 59.3)
- moved C48 72.6 mm to (157.9, 61.4)
- moved C34 64.6 mm to (142.6, 57.6), turned to 90 degrees
- moved U9 63.9 mm to (145.2, 57.4)
- moved R16 63.4 mm to (149.9, 63.3)
- moved R37 63.4 mm to (149.9, 62.2)
- moved TP15 63.4 mm to (142.0, 60.9)
- moved C12 63.4 mm to (148.1, 64.8)
- moved C39 63.4 mm to (145.7, 64.0)
- moved C43 63.4 mm to (146.7, 59.7)
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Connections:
- R18 pad 1: /ESP32/5V_SWITCH -> /ASIC/5V_SWITCH
- U2 pad 7: /ASIC/1V2 -> /ASIC/1V2_0
- U2 pad 8: /ASIC/1V2 -> /ASIC/1V2_0
- U6 pad 36: /ESP32/P_RX -> unconnected-(U6-U0RXD/GPIO44/CLK_OUT2-Pad36)
- U6 pad 37: /ESP32/P_TX -> unconnected-(U6-U0TXD/GPIO43/CLK_OUT1-Pad37)
- U6 pad 38: /VDD -> unconnected-(U6-GPIO2/TOUCH2/ADC1_CH1-Pad38)
- U9 pad 6: /ESP32/5V_SWITCH -> /ASIC/5V_SWITCH
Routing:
- net /ASIC/5V_SWITCH: track 0.00 -> 171.0 mm, vias 0 -> 7
- net /3V3: track 14.2 -> 86.4 mm, vias 5 -> 7
- net (no net): track 62.1 -> 0.00 mm, vias 1 -> 0
- net /ASIC/1V2_1: track 0.00 -> 51.2 mm, vias 0 -> 10
- net /VDD: track 42.8 -> 0.05 mm
- net /ASIC/RST_3V3: track 0.70 -> 42.3 mm, vias 1 -> 2
- net /ASIC/TX_3V3: track 16.8 -> 55.9 mm
- net /ASIC/RX_3V3: track 15.5 -> 54.4 mm
- net /ASIC/1V2_0: track 5.59 -> 39.2 mm, vias 1 -> 5
- net /ASIC/Level Shifter/CLKI: track 0.00 -> 32.8 mm, vias 0 -> 1
- net /ESP32/P_TX: track 32.2 -> 0.00 mm, vias 1 -> 0
- net /12V: track 0.01 -> 31.8 mm, vias 0 -> 12
- net /ESP32/P_RX: track 30.8 -> 0.00 mm, vias 3 -> 0
- net /ASIC/Level Shifter/BI: track 0.00 -> 30.4 mm, vias 0 -> 2
- net /ASIC/Level Shifter/CI2: track 0.00 -> 30.4 mm, vias 0 -> 1
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- added copper zone on In2.Cu, net /12V
- added copper zone on B.Cu, net /ASIC/5V_SWITCH
